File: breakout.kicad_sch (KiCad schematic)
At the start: 43 parts, among them J1 Conn_02x05_Odd_Even, J10 SATA_Power_15P_Male, J2 USB_C_Receptacle_USB2.0_16P, J7 SATA_Power_15P_Male, J8 SATA_Power_15P_Male, J9 SATA_Power_15P_Male, Q1 DMP3013SFV, Q2 DMP3013SFV, SW1 SW_DPST_x2, U1 TPS568230, U2 CYPD3174-24LQXQ

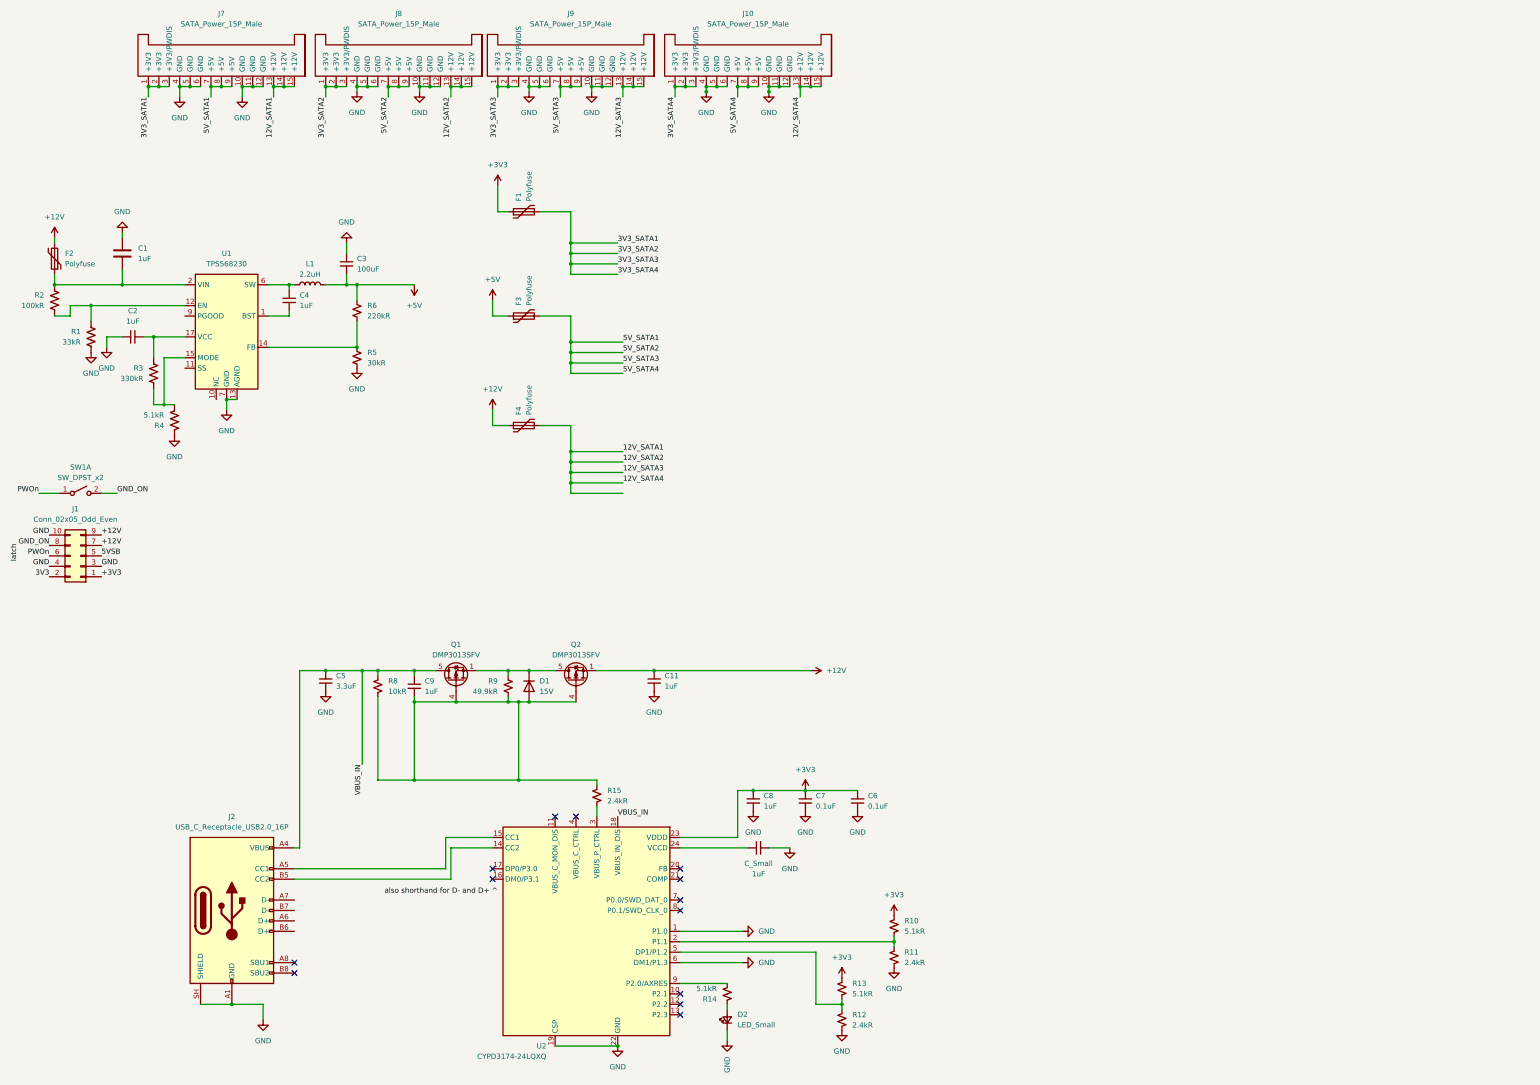
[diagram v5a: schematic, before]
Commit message: pullup/down on IC s.t. 12v 4a max
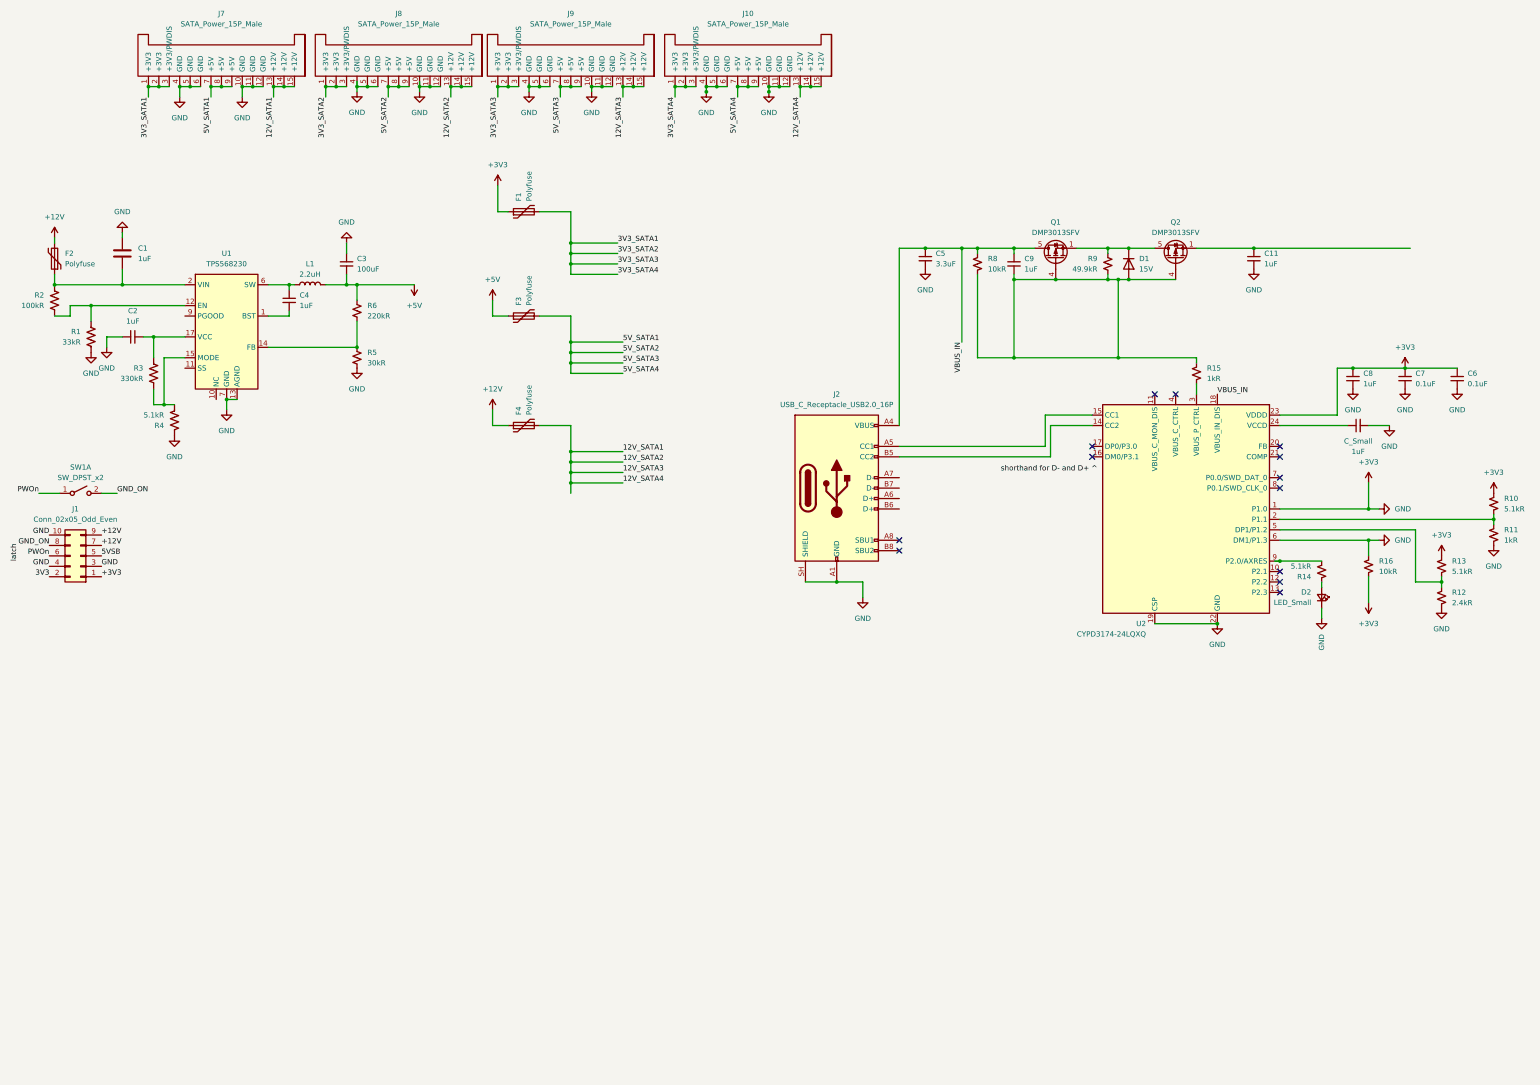
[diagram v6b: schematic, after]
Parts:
- added R16: 10kR, symbol Device:R_Small_US
- R11, R15: value 2.4kR -> 1kR
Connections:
- net GND is gone; now on net +3V3: 1uF.2, C1.1, C11.2, C2.1, C3.1, C5.2, C6.2, C7.2, C8.2, D2.1 (K), J1.10 (Pin_10), J1.3 (Pin_3), J1.4 (Pin_4), J10.10 (GND), J10.11 (GND), J10.12 (GND), J10.4 (GND), J10.5 (GND), J10.6 (GND), J2.A1 (GND), J2.A12 (GND), J2.B1 (GND), J2.B12 (GND), J2.SH (SHIELD), J7.10 (GND), J7.11 (GND), J7.12 (GND), J7.4 (GND), J7.5 (GND), J7.6 (GND), J8.10 (GND), J8.11 (GND), J8.12 (GND), J8.4 (GND), J8.5 (GND), J8.6 (GND), J9.10 (GND), J9.11 (GND), J9.12 (GND), J9.4 (GND), J9.5 (GND), J9.6 (GND), R1.2, R11.2, R12.2, R4.1, R5.2, U1.13 (AGND), U1.18 (GND), U1.21 (GND), U1.7 (GND), U1.8 (GND), U2.1 (P1.0), U2.19 (CSP), U2.22 (GND), U2.25 (GND), U2.6 (DM1/P1.3)
- net +12V: no longer C11.1, Q2.1 (S), Q2.2 (S), Q2.3 (S)
- net +3V3: now also R16.1, R16.2
- new net: C11.1, Q2.1 (S), Q2.2 (S), Q2.3 (S)
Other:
- moved on the sheet: 1uF, C11, C5, C6, C7, C8, C9, D1, D2, J2, Q1, Q2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
